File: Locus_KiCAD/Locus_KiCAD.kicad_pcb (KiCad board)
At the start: 2 copper layers, 71 x 73 mm, 9 parts, among them J1 LifePo4 (Vin), J2 BMS, J3 TP5000, J4 Barrel_Jack_Switch, J5 Screw_Terminal_01x04, U1 ESP32-DevKit-USB-C

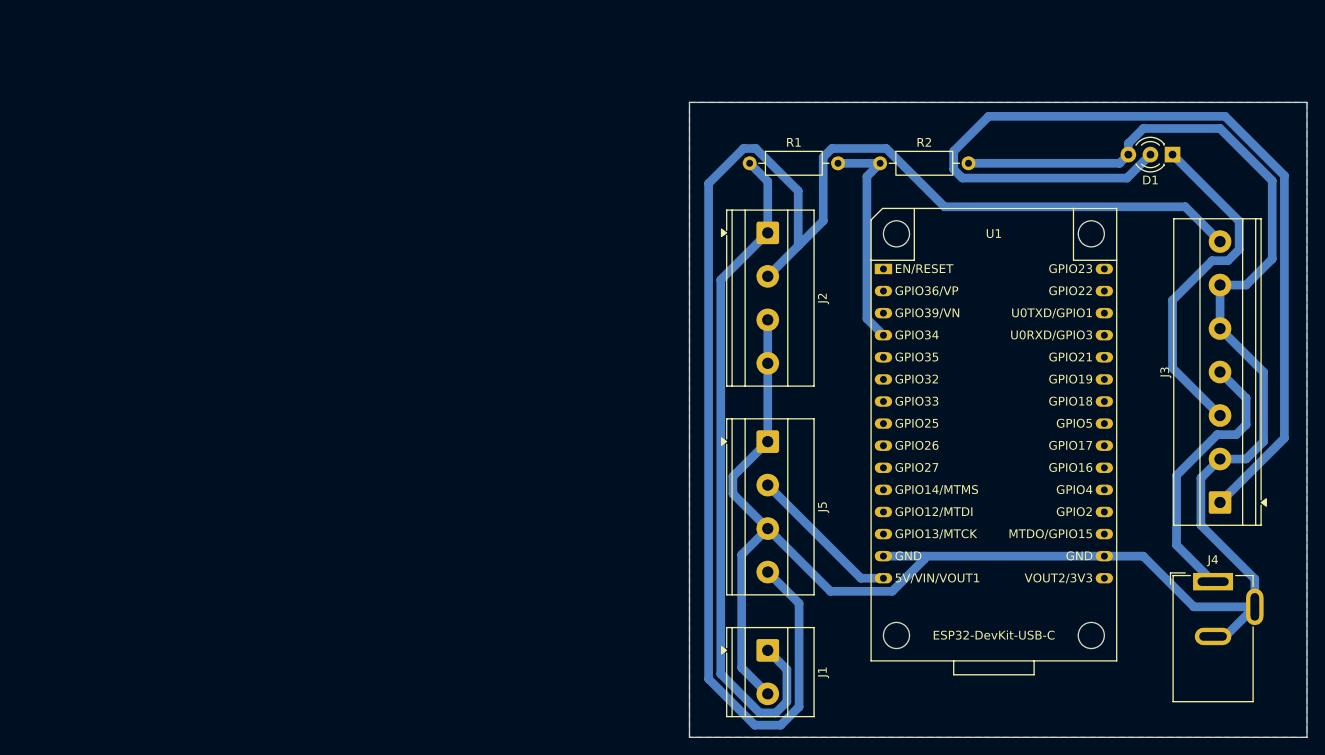
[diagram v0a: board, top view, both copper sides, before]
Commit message: Changed schema and pcb model. Added esp 32 model
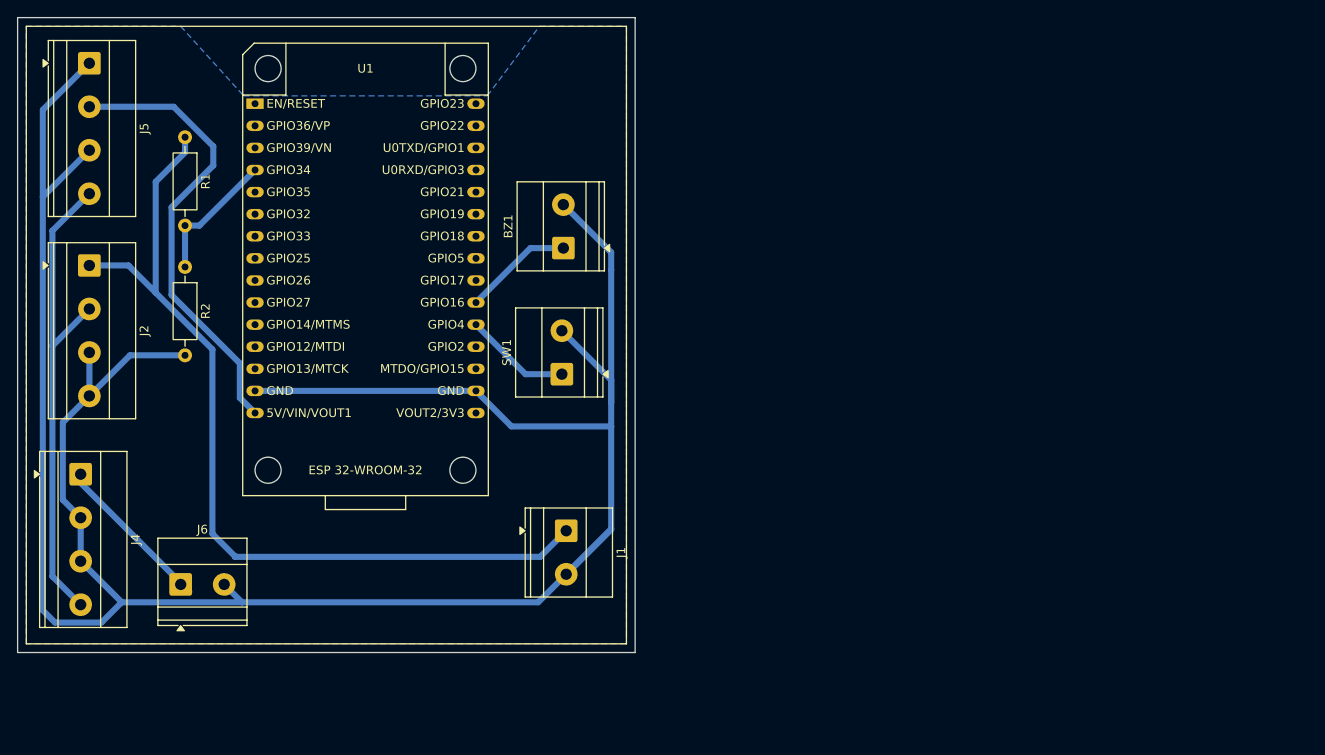
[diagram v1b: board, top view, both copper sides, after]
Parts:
- removed D1: LED_Dual_AAK, LED_THT:LED_D3.0mm-3
- removed J3: TP5000, TerminalBlock_Phoenix:TerminalBlock_Phoenix_MKDS-1,5-7_1x07_P5.00mm_Horizontal
- added BZ1: Buzzer, TerminalBlock_Phoenix:TerminalBlock_Phoenix_MKDS-1,5-2_1x02_P5.00mm_Horizontal, F.Cu at (95.5, 78.8)
- added J6: DC JACK, TerminalBlock_Phoenix:TerminalBlock_Phoenix_MKDS-1,5-2_1x02_P5.00mm_Horizontal, F.Cu at (51.5, 117.4)
- added SW1: EMERGENCY BUTTON, TerminalBlock_Phoenix:TerminalBlock_Phoenix_MKDS-1,5-2_1x02_P5.00mm_Horizontal, F.Cu at (95.3, 93.2)
- J4: value Barrel_Jack_Switch -> TP5000; footprint Connector_BarrelJack:BarrelJack_GCT_DCJ200-10-A_Horizontal -> TerminalBlock_Phoenix:TerminalBlock_Phoenix_MKDS-1,5-4_1x04_P5.00mm_Horizontal
- J5: value Screw_Terminal_01x04 -> MT3068
- U1: value ESP32-DevKit-USB-C -> ESP 32-WROOM-32
- moved J4 130.8 mm to (40.0, 104.8), turned to -90 degrees
- moved J5 89.3 mm to (41.0, 57.5)
- moved R2 80.8 mm to (52.0, 80.9), turned to -90 degrees
- moved J2 78.1 mm to (41.0, 80.8)
- moved U1 74.7 mm to (60.0, 62.1)
- moved R1 65.0 mm to (52.0, 66.0), turned to -90 degrees
- moved J1 26.9 mm to (95.8, 111.2)
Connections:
- U1 pad 20: unconnected-(U1-ADC2_CH0/GPIO4-Pad20) -> Net-(U1-ADC2_CH0/GPIO4)
- U1 pad 21: unconnected-(U1-GPIO16-Pad21) -> Net-(BZ1-+)
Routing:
- net Net-(J2-Pin_2): track 174.5 -> 56.4 mm
- net Net-(D1-A2): track 109.4 -> 0.00 mm
- net GND: track 225.4 -> 291.8 mm
- net Net-(D1-A1): track 39.7 -> 0.00 mm
- net Net-(J5-Pin_2): track 17.7 -> 52.8 mm
- net Net-(J1-Pin_1): track 78.6 -> 101.7 mm
- net Net-(J4-Pin_1): track 31.7 -> 18.7 mm
- net Net-(BZ1-+): track 0.00 -> 12.6 mm
- net Net-(U1-ADC2_CH0/GPIO4): track 0.00 -> 12.2 mm
- net Net-(U1-VDET_1/GPIO34/ADC1_CH6): track 26.0 -> 15.5 mm

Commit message: v2.0.0 added the 3d model, closer to ending
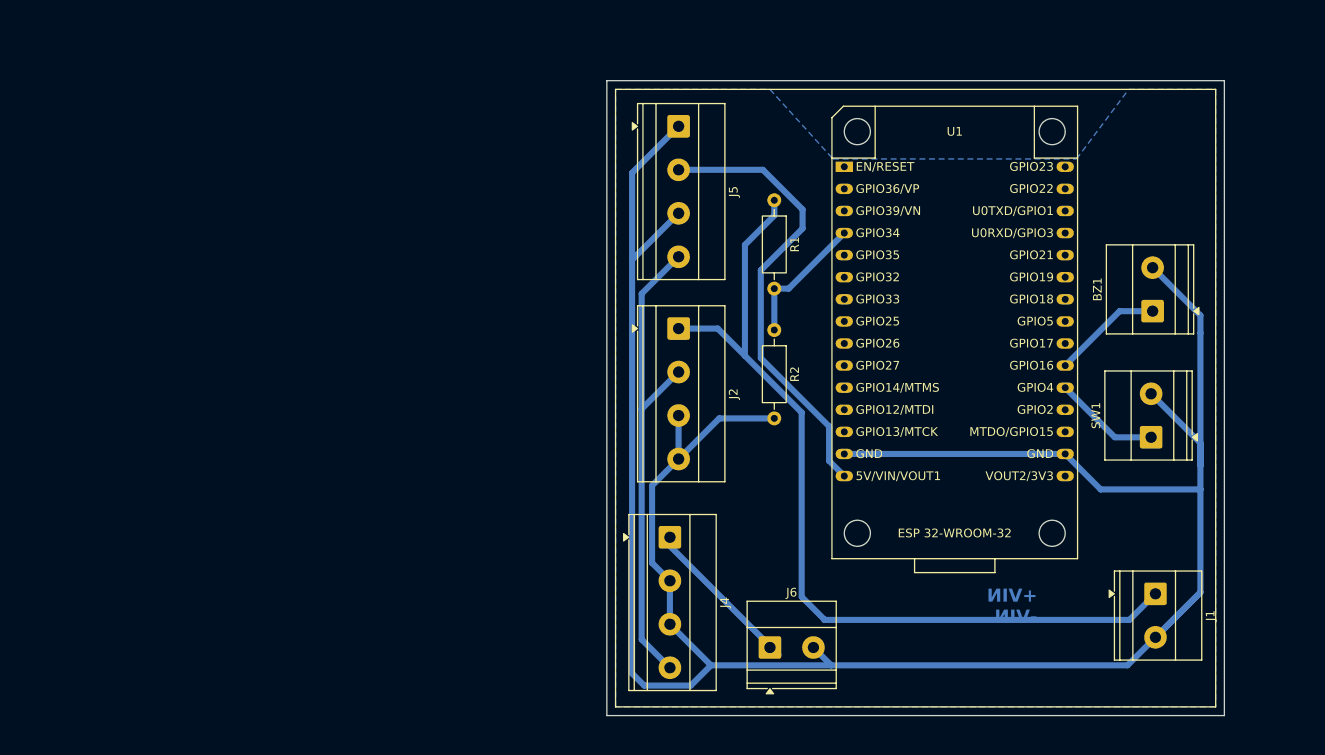
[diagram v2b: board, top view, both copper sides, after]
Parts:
- moved BZ1 68.1 mm to (163.2, 86.0)
- moved J2 68.1 mm to (108.8, 88.0)
- moved J4 68.1 mm to (107.8, 112.0)
- moved J5 68.1 mm to (108.8, 64.8)
- moved J6 68.1 mm to (119.2, 124.7)
- moved R1 68.1 mm to (119.8, 73.2)
- moved R2 68.1 mm to (119.8, 88.2)
- moved U1 68.1 mm to (127.8, 69.4)
- moved J1 68.1 mm to (163.6, 118.5)
- moved SW1 68.1 mm to (163.1, 100.5)
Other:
- board text added: "+VIN -VIN"
